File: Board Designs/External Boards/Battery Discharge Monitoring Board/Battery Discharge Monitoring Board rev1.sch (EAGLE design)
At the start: 67 parts

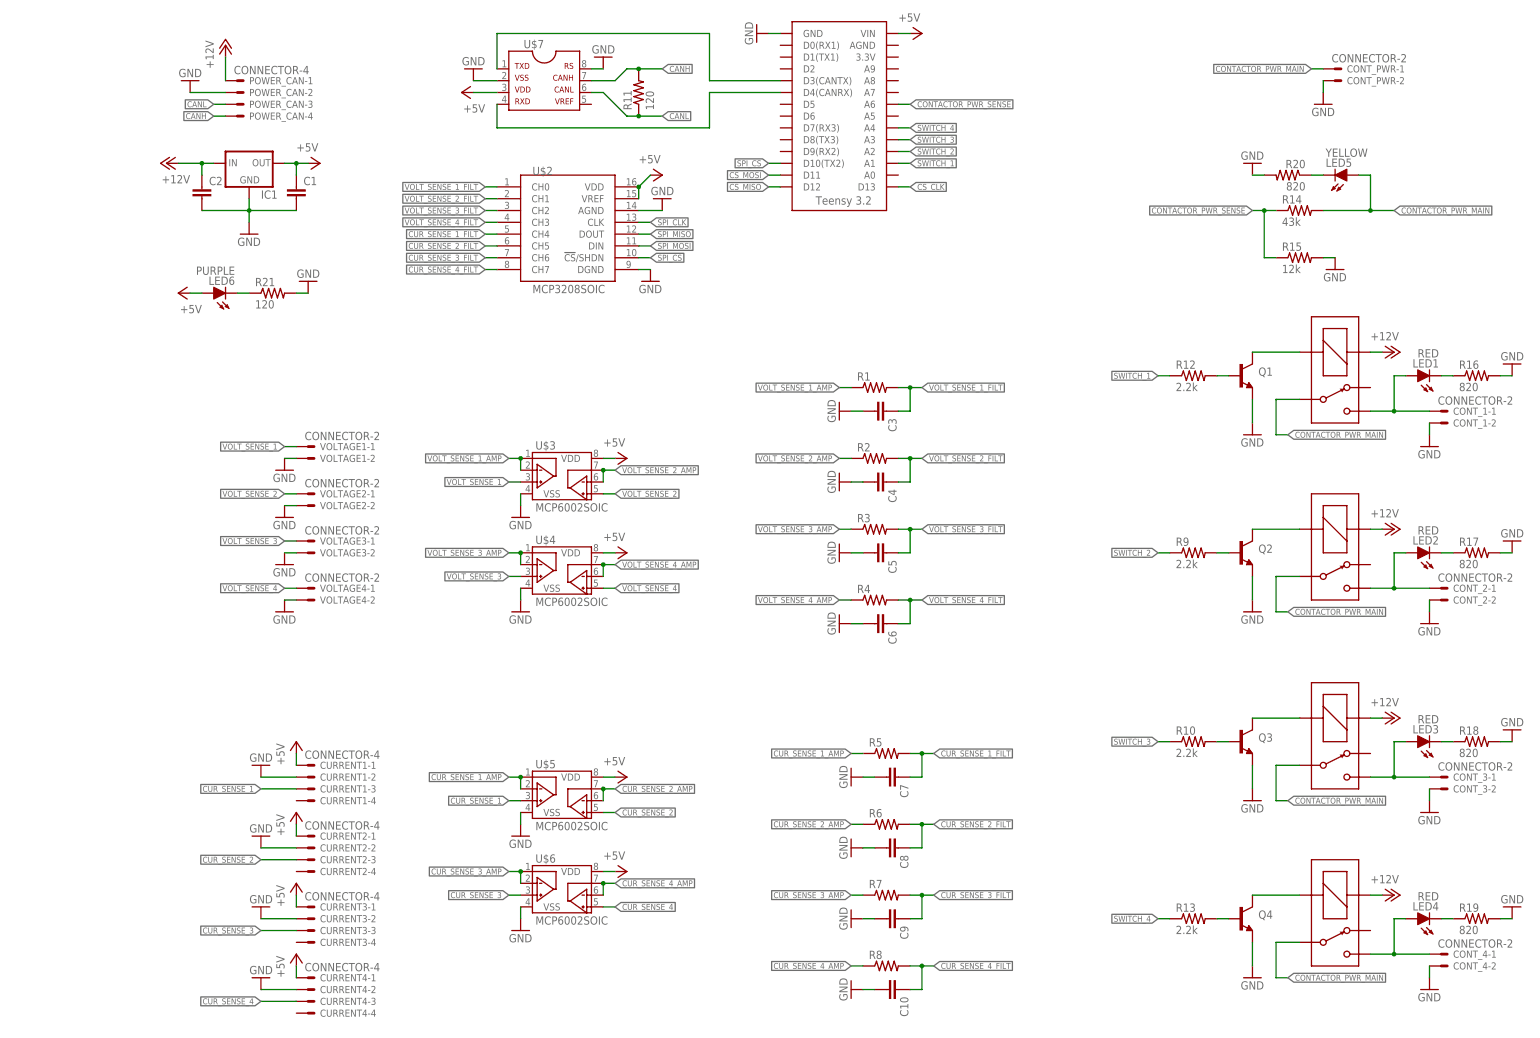
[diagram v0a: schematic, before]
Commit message: Add Molex 14-pin to library, add layout for battery testing board, update silkscreen on BMS adapter board
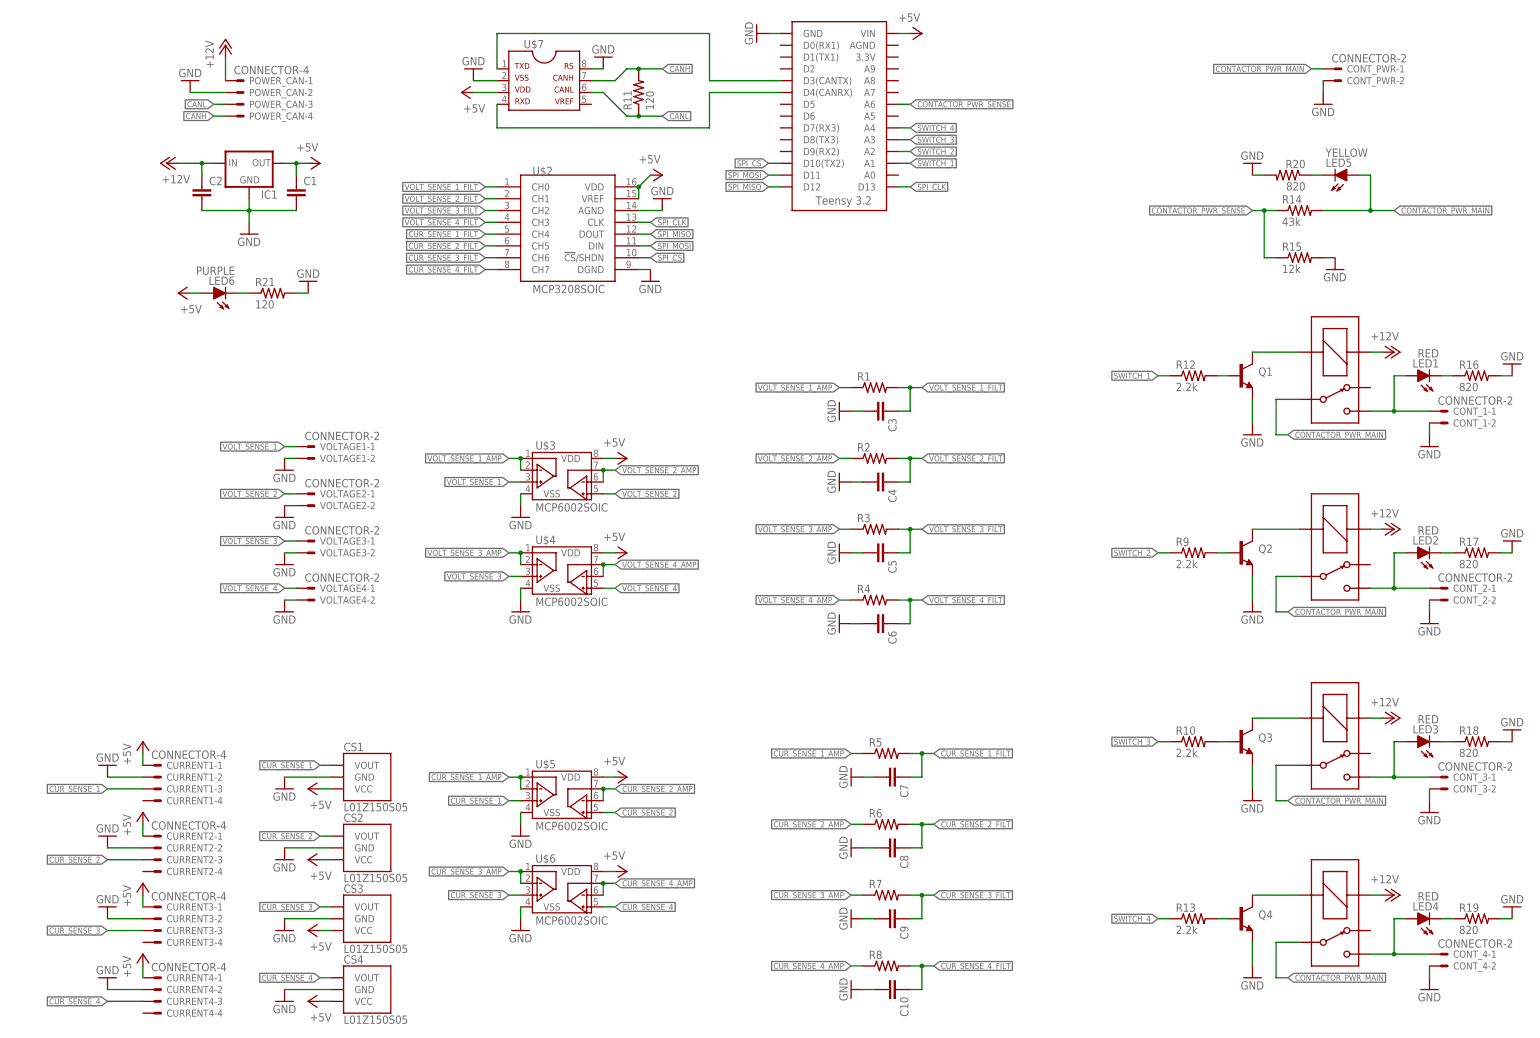
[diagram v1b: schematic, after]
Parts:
- added CS1, CS2, CS3, CS4: L01Z150S05, HyTechDevices:L01Z150S05
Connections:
- removed net CS_CLK: U$1.D13
- removed net CS_MISO: U$1.D12
- removed net CS_MOSI: U$1.D11
- net +5V: now also CS1.VCC, CS2.VCC, CS3.VCC, CS4.VCC
- net CUR_SENSE_1: now also CS1.VOUT
- net CUR_SENSE_2: now also CS2.VOUT
- net CUR_SENSE_3: now also CS3.VOUT
- net CUR_SENSE_4: now also CS4.VOUT
- net GND: now also CS1.GND, CS2.GND, CS3.GND, CS4.GND
- net SPI_CLK: now also U$1.D13
- net SPI_MISO: now also U$1.D12
- net SPI_MOSI: now also U$1.D11
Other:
- moved on the sheet: CURRENT1-1, CURRENT1-2, CURRENT1-3, CURRENT1-4, CURRENT2-1, CURRENT2-2, CURRENT2-3, CURRENT2-4, CURRENT3-1, CURRENT3-2, CURRENT3-3, CURRENT3-4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

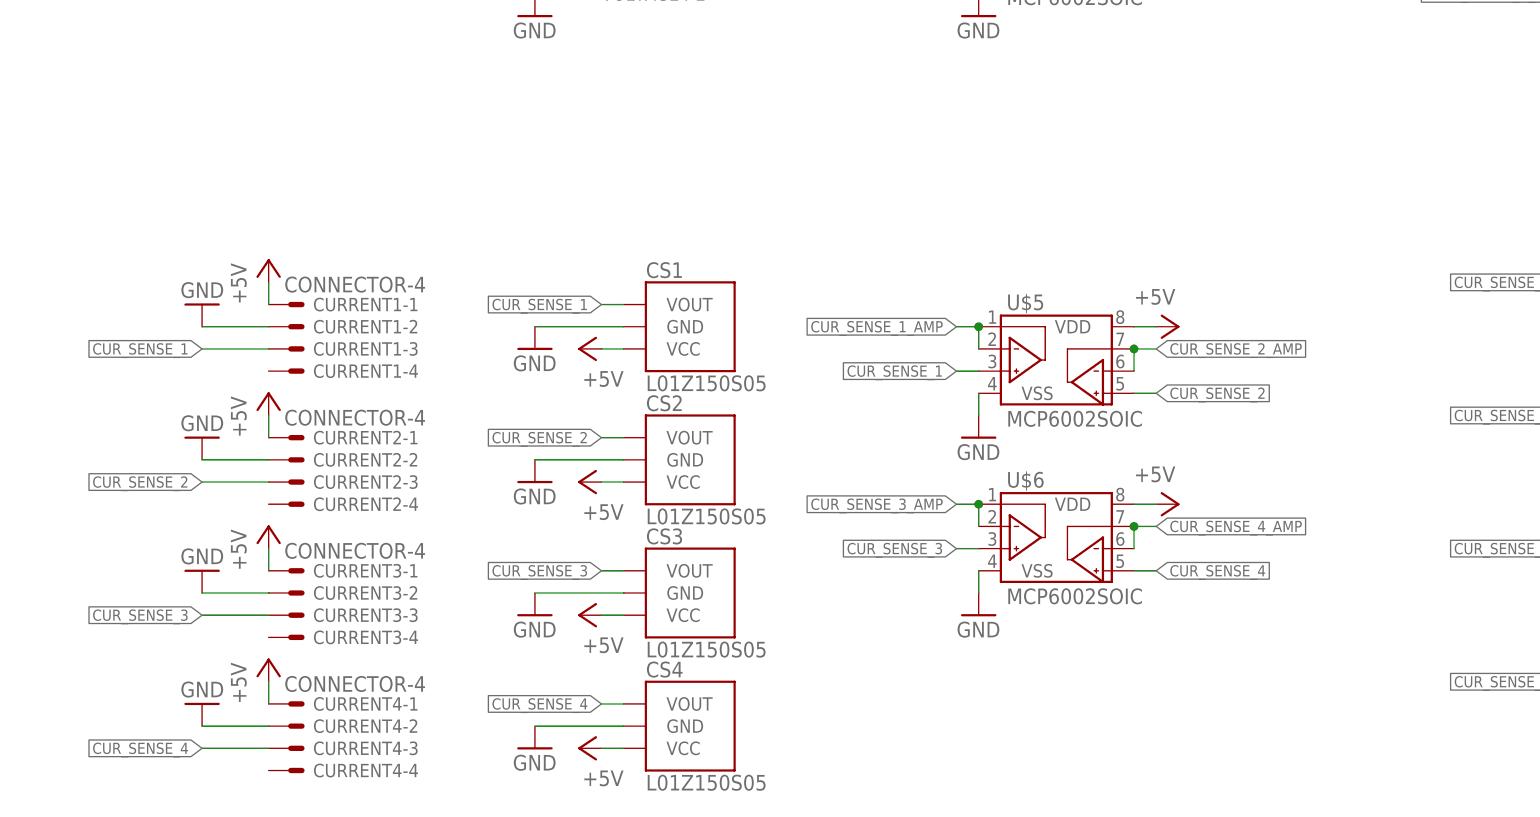
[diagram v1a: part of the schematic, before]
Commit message: Add 10k resistors to current sensors, fix DRC errors, small silkscreen tweaks for mfg
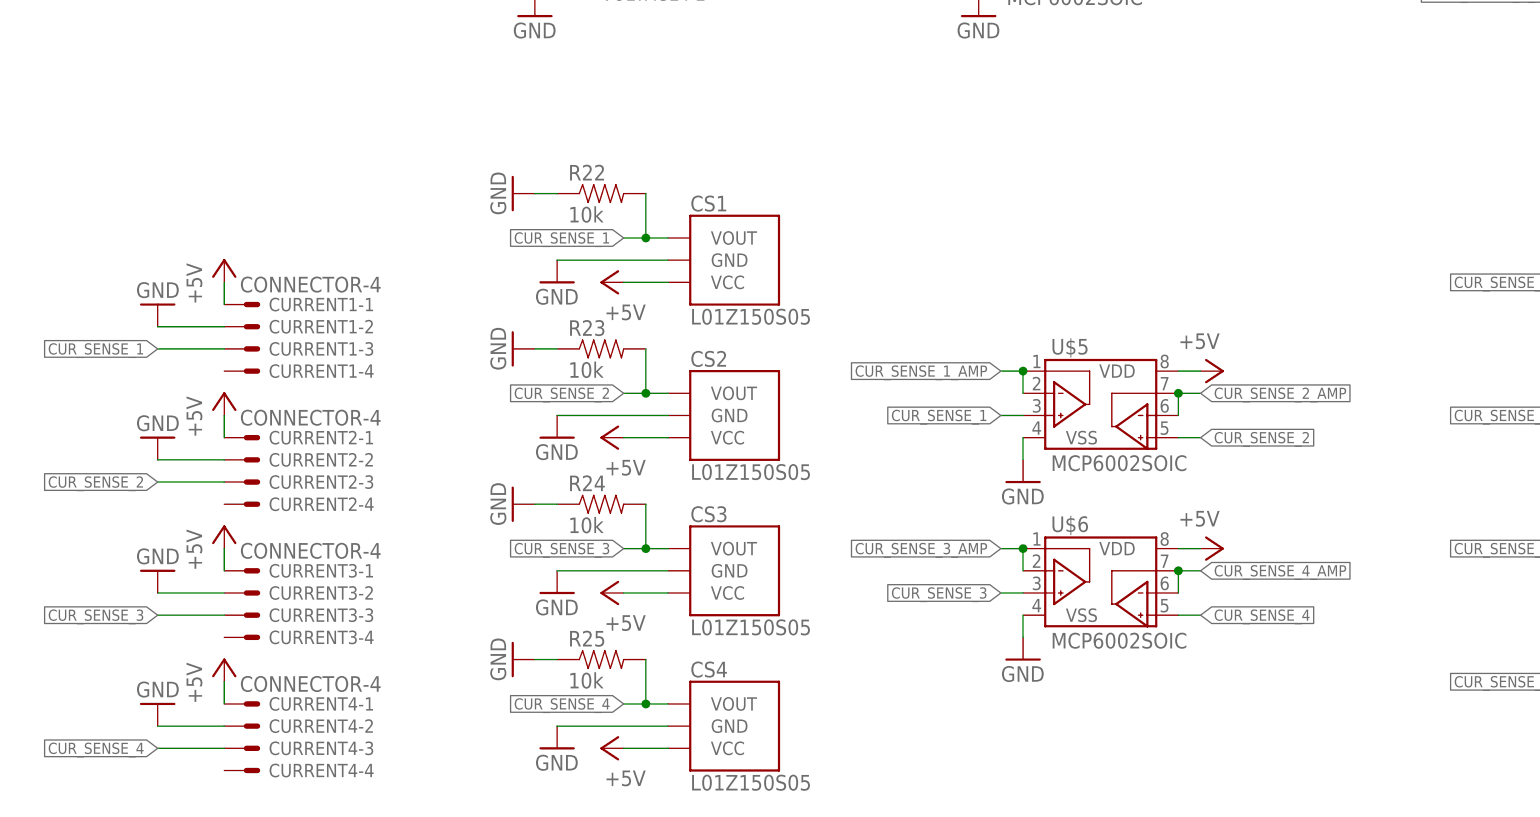
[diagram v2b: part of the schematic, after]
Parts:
- added R22, R23, R24, R25: 10k, HyTechDevices:RESISTOR0805-RES
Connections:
- net CUR_SENSE_1: now also R22.2
- net CUR_SENSE_2: now also R23.2
- net CUR_SENSE_3: now also R24.2
- net CUR_SENSE_4: now also R25.2
- net GND: now also R22.1, R23.1, R24.1, R25.1
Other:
- moved on the sheet: CS1, CS2, CS3, CS4, CURRENT1-1, CURRENT1-2, CURRENT1-3, CURRENT1-4, CURRENT2-1, CURRENT2-2, CURRENT2-3, CURRENT2-4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

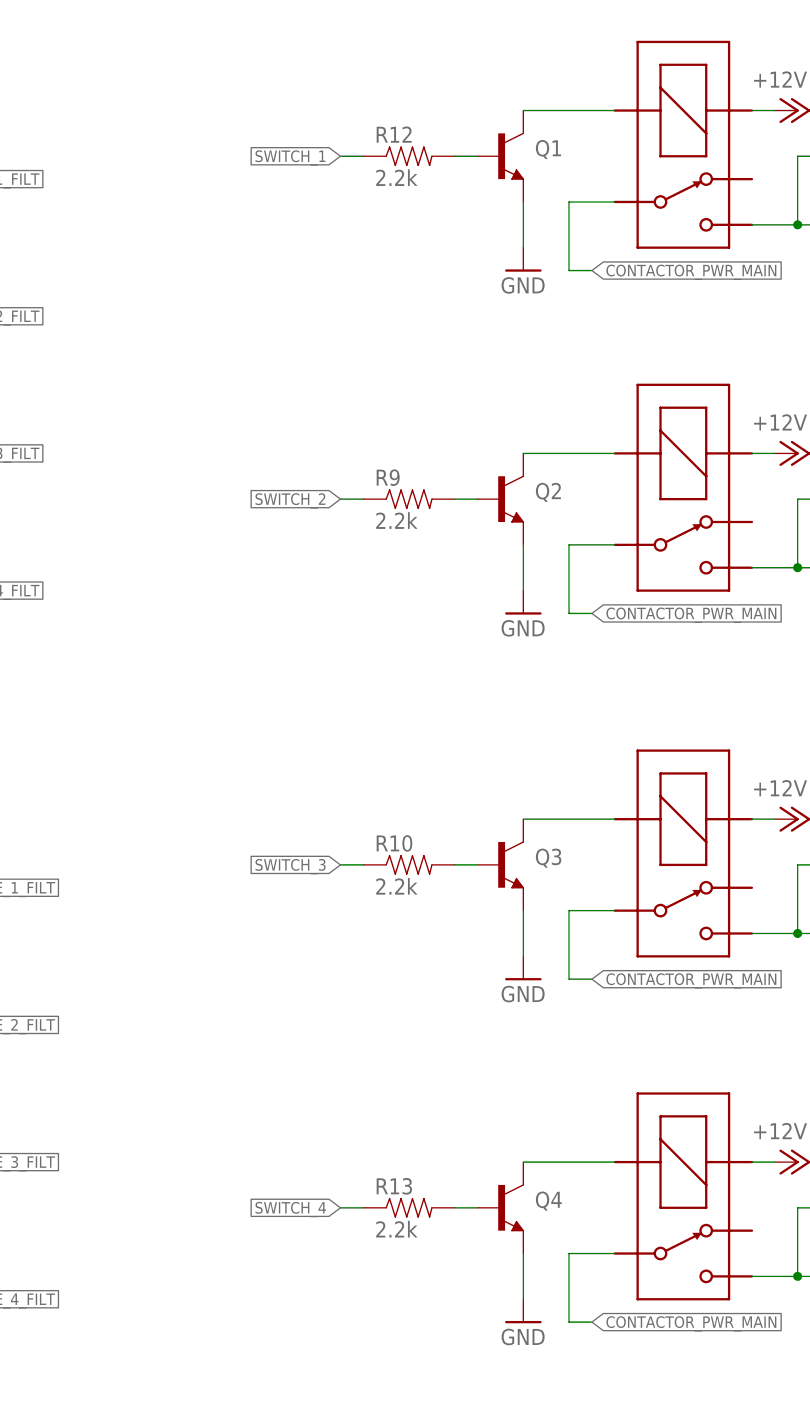
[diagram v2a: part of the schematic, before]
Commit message: Updated resistor values for BJTs
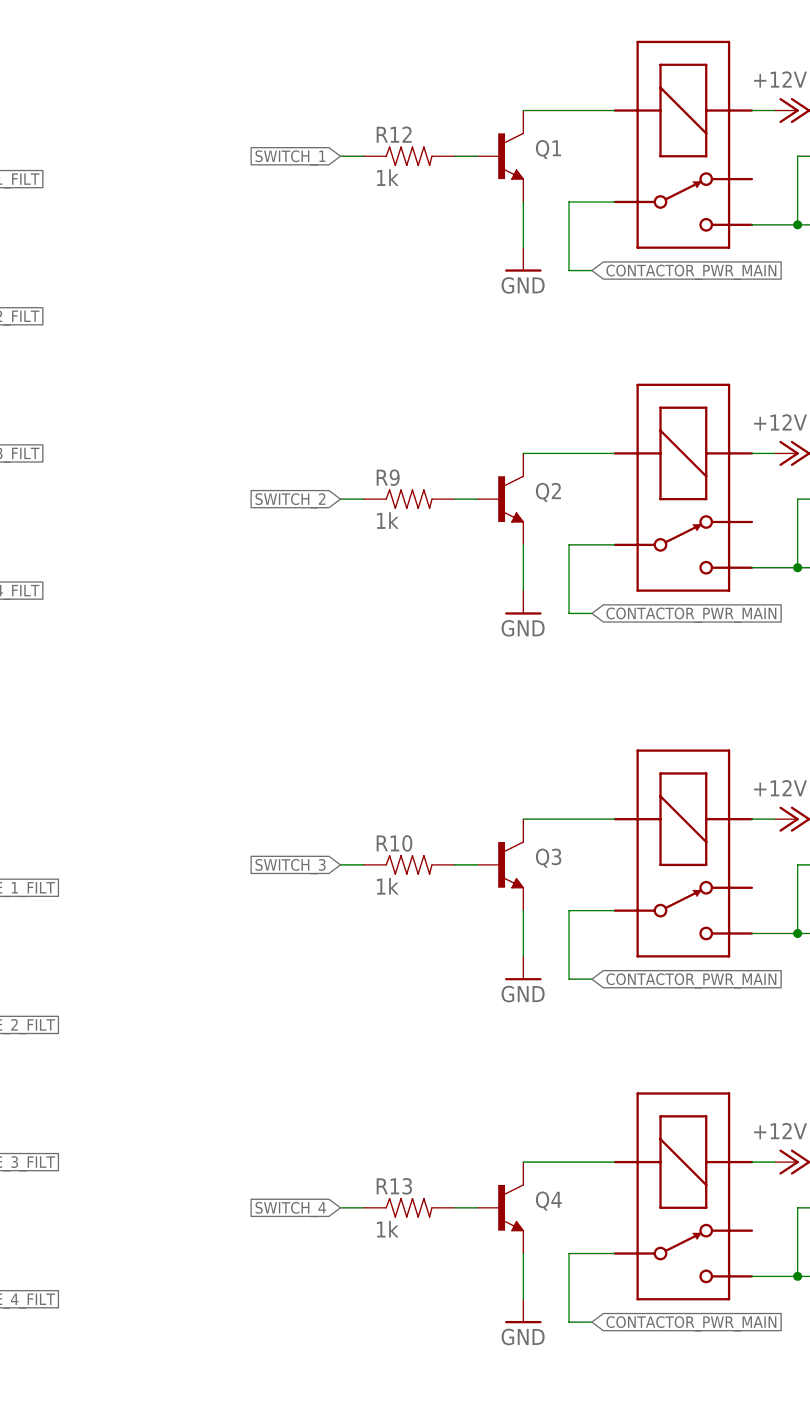
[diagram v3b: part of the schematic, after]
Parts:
- R10, R12, R13, R9: value 2.2k -> 1k
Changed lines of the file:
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@@
 <drawing>
 <settings>
-<setting alwaysvectorfont="no"/>
+<setting alwaysvectorfont="yes"/>
 <setting verticaltext="up"/>
 </settings>
-<grid distance="0.1" unitdist="inch" unit="inch" style="lines" multiple="1" display="no" altdistance="0.01" altunitdist="inch" altunit="inch"/>
+<grid distance="0.1" unitdist="inch" unit="inch" style="lines" multiple="1" display="yes" altdistance="0.01" altunitdist="inch" altunit="inch"/>
 <layers>
 <layer number="1" name="Top" color="4" fill="1" visible="no" active="no"/>
@@
 <part name="R11" library="HyTechDevices" deviceset="RESISTOR" device="0805-RES" value="120"/>
 <part name="Q1" library="HyTechDevices" deviceset="BJT_NPN" device="SOT"/>
-<part name="R12" library="HyTechDevices" deviceset="RESISTOR" device="0805-RES" value="2.2k"/>
+<part name="R12" library="HyTechDevices" deviceset="RESISTOR" device="0805-RES" value="1k"/>
 <part name="GND29" library="supply1" library_urn="urn:adsk.eagle:library:371" deviceset="GND" device=""/>
 <part name="U$8" library="HyTechDevices" deviceset="G5LE" device=""/>
@@
 <part name="GND26" library="supply1" library_urn="urn:adsk.eagle:library:371" deviceset="GND" device=""/>
 <part name="Q2" library="HyTechDevices" deviceset="BJT_NPN" device="SOT"/>
-<part name="R9" library="HyTechDevices" deviceset="RESISTOR" device="0805-RES" value="2.2k"/>
+<part name="R9" library="HyTechDevices" deviceset="RESISTOR" device="0805-RES" value="1k"/>
 <part name="GND31" library="supply1" library_urn="urn:adsk.eagle:library:371" deviceset="GND" device=""/>
 <part name="U$9" library="HyTechDevices" deviceset="G5LE" device=""/>
@@
 <part name="GND32" library="supply1" library_urn="urn:adsk.eagle:library:371" deviceset="GND" device=""/>
 <part name="Q3" library="HyTechDevices" deviceset="BJT_NPN" device="SOT"/>
-<part name="R10" library="HyTechDevices" deviceset="RESISTOR" device="0805-RES" value="2.2k"/>
+<part name="R10" library="HyTechDevices" deviceset="RESISTOR" device="0805-RES" value="1k"/>
 <part name="GND33" library="supply1" library_urn="urn:adsk.eagle:library:371" deviceset="GND" device=""/>
 <part name="U$10" library="HyTechDevices" deviceset="G5LE" device=""/>
@@
 <part name="GND34" library="supply1" library_urn="urn:adsk.eagle:library:371" deviceset="GND" device=""/>
 <part name="Q4" library="HyTechDevices" deviceset="BJT_NPN" device="SOT"/>
-<part name="R13" library="HyTechDevices" deviceset="RESISTOR" device="0805-RES" value="2.2k"/>
+<part name="R13" library="HyTechDevices" deviceset="RESISTOR" device="0805-RES" value="1k"/>
 <part name="GND35" library="supply1" library_urn="urn:adsk.eagle:library:371" deviceset="GND" device=""/>
 <part name="U$11" library="HyTechDevices" deviceset="G5LE" device=""/>
